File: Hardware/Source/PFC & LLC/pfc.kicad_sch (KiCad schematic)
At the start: 70 parts, among them J1 HB9500M-9.5-3P, K1 Relay 12VDC 10A, Q1 MMBT2222A, Q2 IPP60R125CP, Q3 MMBT2222A, U1 PC817X2NIPW, U2 OPAMP_OP07CSZ, U3 UCC28180D, U4 SN74LVC1G14DBVR

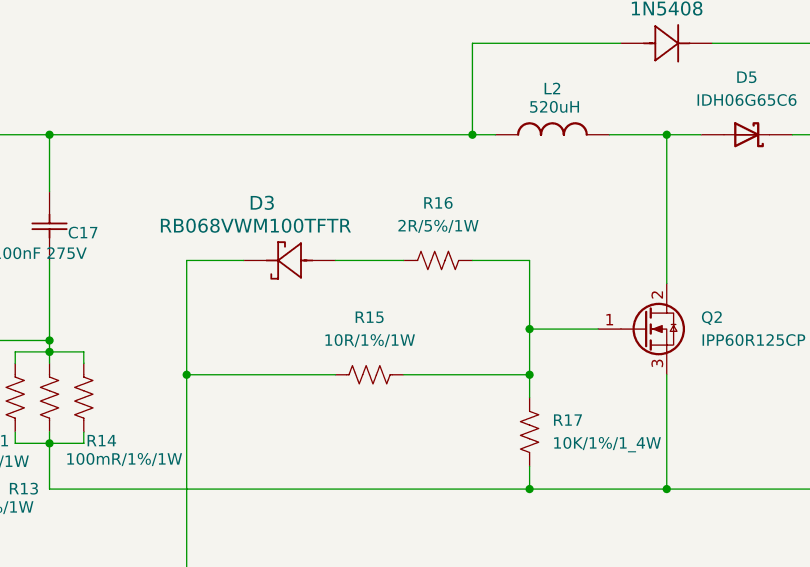
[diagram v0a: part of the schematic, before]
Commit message: Update PFC&LLC
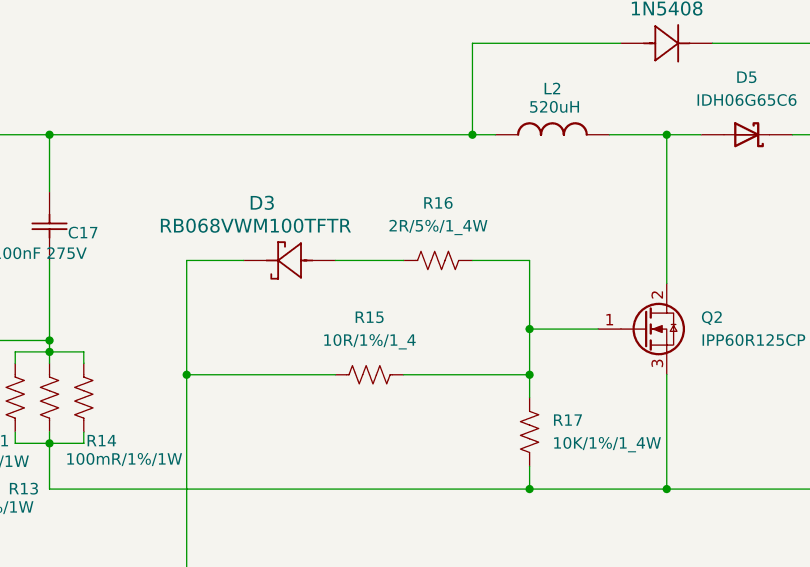
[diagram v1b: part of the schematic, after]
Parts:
- removed R15: 10R/1%/1W, charge_battery_footprint_lib:Res_2512, symbol charge_battery_sym_lib:Res_10R_2512_1%
- removed R16: 2R/5%/1W, charge_battery_footprint_lib:Res_2512, symbol charge_battery_sym_lib:Res_2R_2512_5%
- added R15: 10R/1%/1_4, charge_battery_footprint_lib:Res_1206, symbol charge_battery_sym_lib:Res_10R_1206_1%
- added R16: 2R/5%/1_4W, charge_battery_footprint_lib:Res_1206, symbol charge_battery_sym_lib:Res_2R_1206_1%
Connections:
- net at D3.1, U3.8 (GATE): now also R15.1
- net at D3.2: now also R16.1
- net at Q2.1 (G), R17.2: now also R15.2, R16.2
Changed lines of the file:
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@@
+	)
+	(symbol
+		(lib_id "charge_battery_sym_lib:Res_10R_1206_1%")
+		(at 313.69 105.41 0)
+		(unit 1)
+		(exclude_from_sim no)
+		(in_bom yes)
+		(on_board yes)
+		(dnp no)
+		(fields_autoplaced yes)
+		(property "Reference" "R15"
+			(at 317.5 99.06 0)
+			(effects
+				(font
+					(size 1.27 1.27)
+				)
+			)
+		)
+		(property "Value" "10R/1%/1_4"
+			(at 317.5 101.6 0)
+			(effects
+				(font
+					(size 1.27 1.27)
+				)
+			)
+		)
+		(property "Footprint" "charge_battery_footprint_lib:Res_1206"
+			(at 331.978 120.904 0)
+			(effects
+				(font
+					(size 1.27 1.27)
+				)
+				(hide yes)
+			)
+		)
+		(property "Datasheet" ""
+			(at 321.31 120.65 0)
+			(effects
+				(font
+					(size 1.27 1.27)
+				)
+				(hide yes)
+			)
+		)
+		(property "Description" "Res 10 Ohm 1206 1%"
+			(at 327.406 121.412 0)
+			(effects
+				(font
+					(size 1.27 1.27)
+				)
+				(hide yes)
+			)
+		)
+		(property "Supply name" "Thegioiic"
+			(at 332.994 121.158 0)
+			(effects
+				(font
+					(size 1.27 1.27)
+				)
+				(hide yes)
+			)
+		)
+		(property "Supply part number" "Điện Trở 10 Ohm 1206 1%"
+			(at 334.01 120.904 0)
+			(effects
+				(font
+					(size 1.27 1.27)
+				)
+				(hide yes)
+			)
+		)
+		(property "Supply URL" "https://www.thegioiic.com/dien-tro-10-ohm-1206-1-"
+			(at 341.122 122.174 0)
+			(effects
+				(font
+					(size 1.27 1.27)
+				)
+				(hide yes)
+			)
+		)
+		(pin "1"
+		)
+		(pin "2"
+		)
+		(instances
+			(project ""
+				(path "/97d1a1fe-d5a5-4da8-b78a-88a9132d14ad/bb0951d9-6e6a-40f4-8bc1-318f9d0bfafc"
+					(reference "R15")
+					(unit 1)
+				)
+			)
+		)
 	)
 	(symbol
@@
 	)
 	(symbol
+		(lib_id "charge_battery_sym_lib:Res_2R_1206_1%")
+		(at 325.12 88.9 0)
+		(unit 1)
+		(exclude_from_sim no)
+		(in_bom yes)
+		(on_board yes)
+		(dnp no)
+		(fields_autoplaced yes)
+		(property "Reference" "R16"
+			(at 325.12 86.36 0)
+			(effects
+				(font
+					(size 1.27 1.27)
+				)
+			)
+		)
+		(property "Value" "2R/5%/1_4W"
+			(at 325.12 88.9 0)
+			(effects
+				(font
+					(size 1.27 1.27)
+				)
+			)
+		)
+		(property "Footprint" "charge_battery_footprint_lib:Res_1206"
+			(at 325.12 88.9 0)
+			(effects
+				(font
+					(size 1.27 1.27)
+				)
+				(hide yes)
+			)
+		)
+		(property "Datasheet" ""
+			(at 325.12 88.9 0)
+			(effects
+				(font
+					(size 1.27 1.27)
+				)
+				(hide yes)
+			)
+		)
+		(property "Description" "Resistor 2 Ohm 1206 5%"
+			(at 325.12 88.9 0)
+			(effects
+				(font
+					(size 1.27 1.27)
+				)
+				(hide yes)
+			)
+		)
+		(property "Supply Name" "thegioiic"
+			(at 325.12 88.9 0)
+			(effects
+				(font
+					(size 1.27 1.27)
+				)
+				(hide yes)
+			)
+		)
+		(property "Supply Part Number" "Điện Trở 2 Ohm 1206 5%"
+			(at 325.12 88.9 0)
+			(effects
+				(font
+					(size 1.27 1.27)
+				)
+				(hide yes)
+			)
+		)
+		(property "Supply URL" "https://www.thegioiic.com/dien-tro-2-ohm-1206-5-"
+			(at 325.12 88.9 0)
+			(effects
+				(font
+					(size 1.27 1.27)
+				)
+				(hide yes)
+			)
+		)
+		(pin "1"
+		)
+		(pin "2"
+		)
+		(instances
+			(project ""
+				(path "/97d1a1fe-d5a5-4da8-b78a-88a9132d14ad/bb0951d9-6e6a-40f4-8bc1-318f9d0bfafc"
+					(reference "R16")
+					(unit 1)
+				)
+			)
+		)
+	)
+	(symbol
 		(lib_id "charge_battery_sym_lib:KBU1010 ")
 		(at 261.62 92.71 90)
@@
 				(path "/97d1a1fe-d5a5-4da8-b78a-88a9132d14ad/bb0951d9-6e6a-40f4-8bc1-318f9d0bfafc"
 					(reference "C1")
-					(unit 1)
-				)
-			)
-		)
-	)
-	(symbol
-		(lib_id "charge_battery_sym_lib:Res_2R_2512_5%")
-		(at 321.31 92.71 0)
-		(unit 1)
-		(exclude_from_sim no)
-		(in_bom yes)
-		(on_board yes)
-		(dnp no)
-		(fields_autoplaced yes)
-		(property "Reference" "R16"
-			(at 325.12 86.36 0)
-			(effects
-				(font
-					(size 1.27 1.27)
-				)
-			)
-		)
-		(property "Value" "2R/5%/1W"
-			(at 325.12 88.9 0)
-			(effects
-				(font
-					(size 1.27 1.27)
-				)
-			)
-		)
-		(property "Footprint" "charge_battery_footprint_lib:Res_2512"
-			(at 339.598 108.204 0)
-			(effects
-				(font
-					(size 1.27 1.27)
-				)
-				(hide yes)
-			)
-		)
-		(property "Datasheet" ""
-			(at 328.93 107.95 0)
-			(effects
-				(font
-					(size 1.27 1.27)
-				)
-				(hide yes)
-			)
-		)
-		(property "Description" "Res 2 Ohm 2512 1%"
-			(at 335.026 108.712 0)
-			(effects
-				(font
-					(size 1.27 1.27)
-				)
-				(hide yes)
-			)
-		)
-		(property "Supply name" "Thegioiic"
-			(at 340.614 108.458 0)
-			(effects
-				(font
-					(size 1.27 1.27)
-				)
-				(hide yes)
-			)
-		)
-		(property "Supply part number" "Điện Trở 2 Ohm 2512 1%"
-			(at 341.63 108.204 0)
-			(effects
-				(font
-					(size 1.27 1.27)
-				)
-				(hide yes)
-			)
-		)
-		(property "Supply URL" "https://www.thegioiic.com/dien-tro-2-ohm-2512-5-"
-			(at 348.742 109.474 0)
-			(effects
-				(font
-					(size 1.27 1.27)
-				)
-				(hide yes)
-			)
-		)
-		(pin "2"
-		)
-		(pin "1"
-		)
-		(instances
-			(project ""
-				(path "/97d1a1fe-d5a5-4da8-b78a-88a9132d14ad/bb0951d9-6e6a-40f4-8bc1-318f9d0bfafc"
-					(reference "R16")
 					(unit 1)
 				)
@@
 					(unit 1)
 				)
-			)
-		)
-	)
-	(symbol
-		(lib_id "charge_battery_sym_lib:Res_10R_2512_1%")
-		(at 313.69 105.41 0)
-		(unit 1)
-		(exclude_from_sim no)
-		(in_bom yes)
-		(on_board yes)
-		(dnp no)
-		(fields_autoplaced yes)
-		(property "Reference" "R15"
-			(at 317.5 99.06 0)
-			(effects
-				(font
-					(size 1.27 1.27)
-				)
-			)
-		)
-		(property "Value" "10R/1%/1W"
-			(at 317.5 101.6 0)
-			(effects
-				(font
-					(size 1.27 1.27)
-				)
-			)
-		)
-		(property "Footprint" "charge_battery_footprint_lib:Res_2512"
-			(at 331.978 120.904 0)
-			(effects
-				(font
-					(size 1.27 1.27)
-				)
-				(hide yes)
-			)
-		)
-		(property "Datasheet" ""
-			(at 321.31 120.65 0)
-			(effects
-				(font
-					(size 1.27 1.27)
-				)
-				(hide yes)
-			)
-		)
-		(property "Description" "Res 10 Ohm 2512 1%"
-			(at 327.406 121.412 0)
-			(effects
-				(font
-					(size 1.27 1.27)
-				)
-				(hide yes)
-			)
-		)
-		(property "Supply name" "Thegioiic"
-			(at 332.994 121.158 0)
-			(effects
-				(font
-					(size 1.27 1.27)
-				)
-				(hide yes)
-			)
-		)
-		(property "Supply part number" "Điện Trở 10 Ohm 2512 1%"
-			(at 334.01 120.904 0)
-			(effects
-				(font
-					(size 1.27 1.27)
-				)
-				(hide yes)
-			)
-		)
-		(property "Supply URL" "https://www.thegioiic.com/dien-tro-10-ohm-2512-1-"
-			(at 341.122 122.174 0)
-			(effects
-				(font
-					(size 1.27 1.27)
-				)
-				(hide yes)
-			)
-		)
-		(pin "2"
-		)
-		(pin "1"
-		)
-		(instances
-			(project ""
-				(path "/97d1a1fe-d5a5-4da8-b78a-88a9132d14ad/bb0951d9-6e6a-40f4-8bc1-318f9d0bfafc"
-					(reference "R15")
-					(unit 1)
-				)

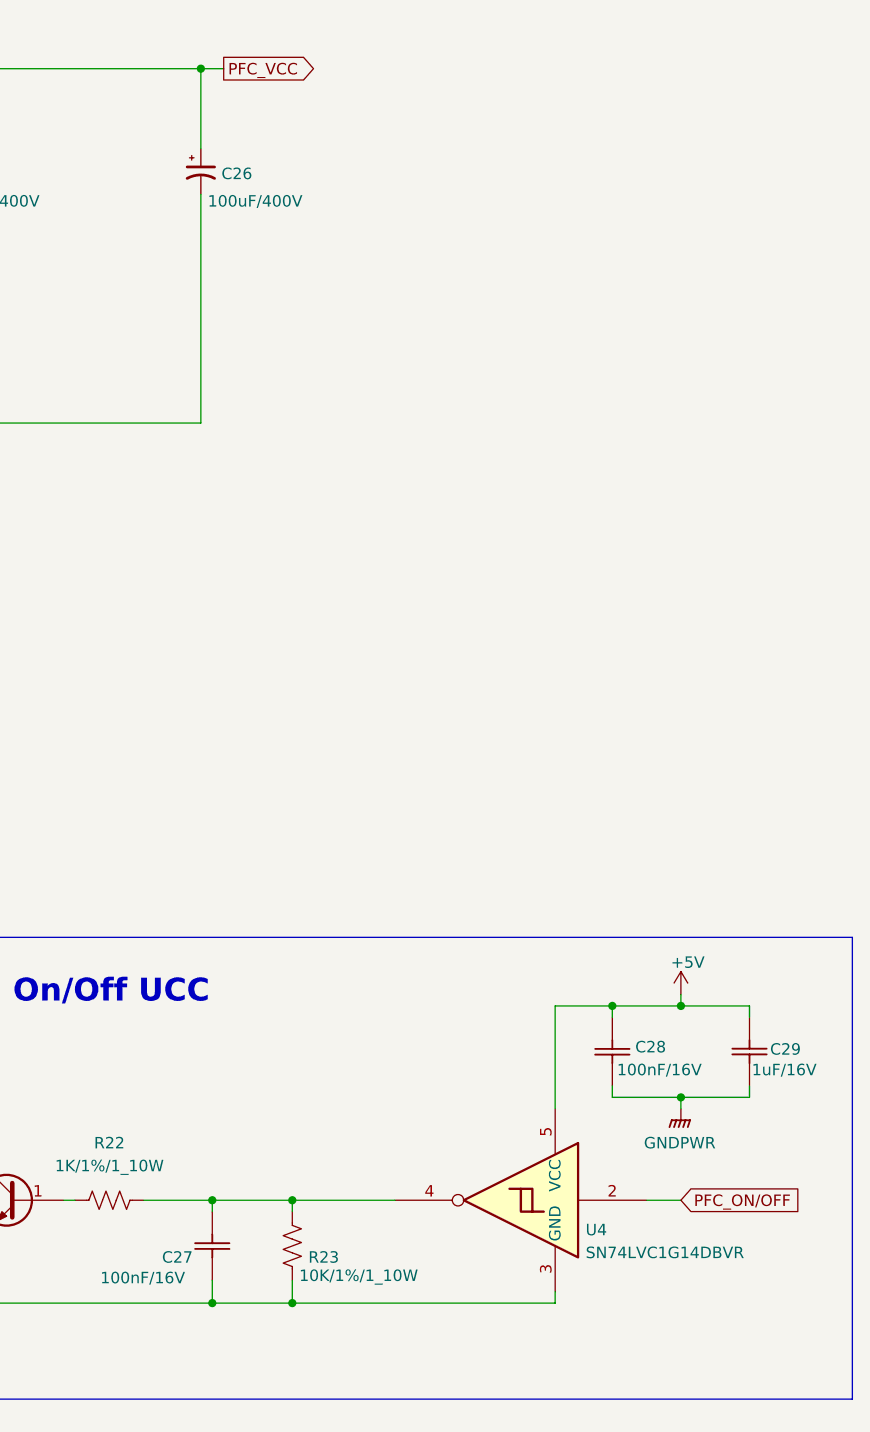
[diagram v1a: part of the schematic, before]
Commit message: Update PFC&LLC
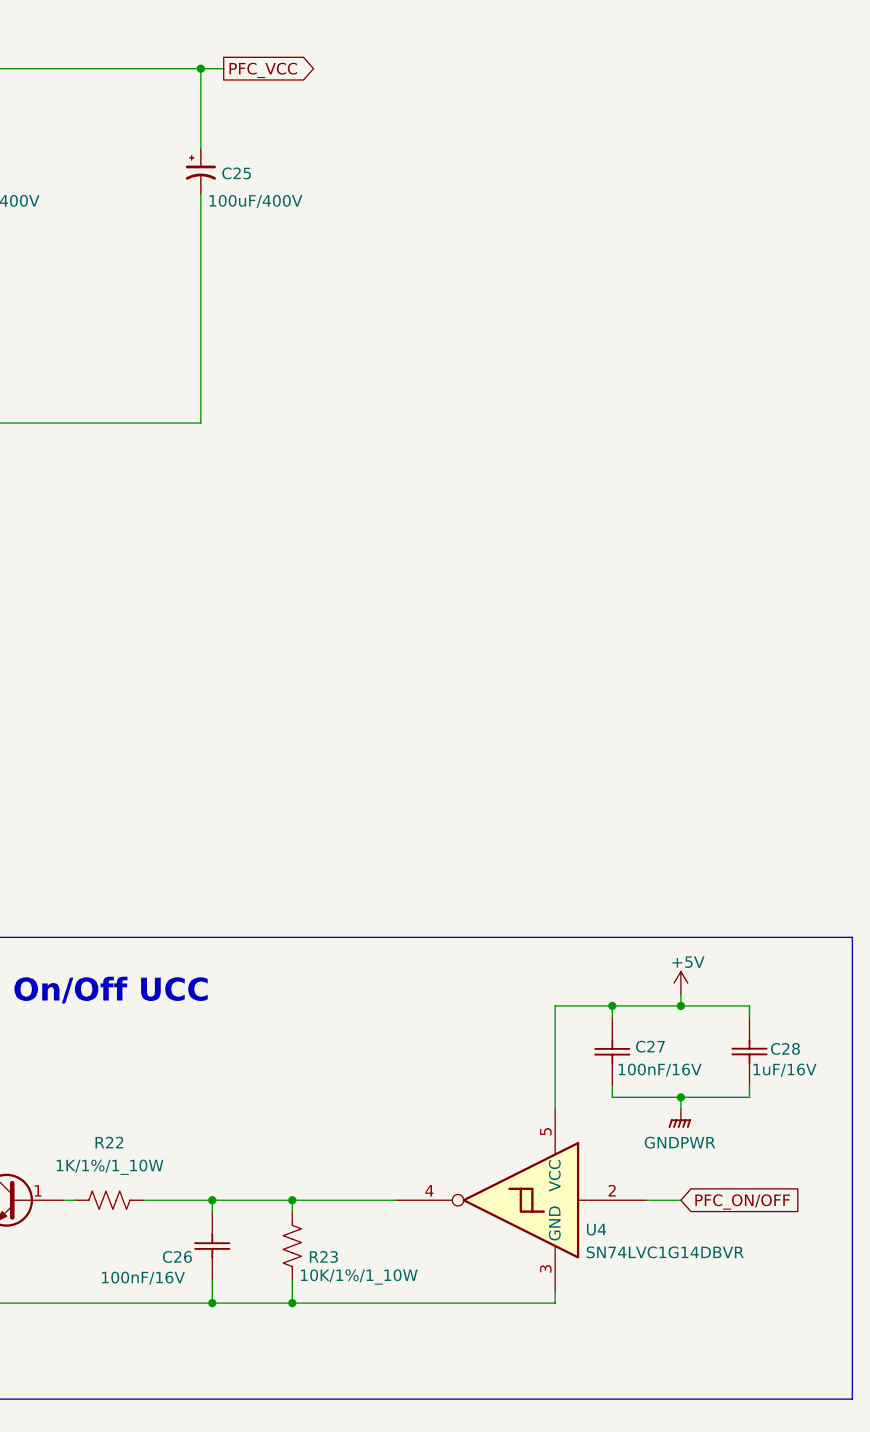
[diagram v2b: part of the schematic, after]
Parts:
- renumbered C26 to C25, C27 to C26, C28 to C27, C29 to C28
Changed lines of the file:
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@@
 		(on_board yes)
 		(dnp no)
-		(property "Reference" "C26"
+		(property "Reference" "C25"
 			(at 429.006 90.424 90)
 			(effects
@@
 			(project "PFC & LLC"
 				(path "/97d1a1fe-d5a5-4da8-b78a-88a9132d14ad/bb0951d9-6e6a-40f4-8bc1-318f9d0bfafc"
-					(reference "C26")
+					(reference "C25")
 					(unit 1)
 				)
@@
 		(on_board yes)
 		(dnp no)
-		(property "Reference" "C28"
+		(property "Reference" "C27"
 			(at 474.98 187.452 90)
 			(effects
@@
 			(project ""
 				(path "/97d1a1fe-d5a5-4da8-b78a-88a9132d14ad/bb0951d9-6e6a-40f4-8bc1-318f9d0bfafc"
-					(reference "C28")
+					(reference "C27")
 					(unit 1)
 				)
@@
 		(on_board yes)
 		(dnp no)
-		(property "Reference" "C29"
+		(property "Reference" "C28"
 			(at 489.966 187.706 90)
 			(effects
@@
 			(project ""
 				(path "/97d1a1fe-d5a5-4da8-b78a-88a9132d14ad/bb0951d9-6e6a-40f4-8bc1-318f9d0bfafc"
-					(reference "C29")
+					(reference "C28")
 					(unit 1)
 				)
@@
 		(on_board yes)
 		(dnp no)
-		(property "Reference" "C27"
+		(property "Reference" "C26"
 			(at 422.402 210.82 90)
 			(effects
@@
 			(project ""
 				(path "/97d1a1fe-d5a5-4da8-b78a-88a9132d14ad/bb0951d9-6e6a-40f4-8bc1-318f9d0bfafc"
-					(reference "C27")
+					(reference "C26")
 					(unit 1)
 				)

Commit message: Update lib: Choke in PFC Circuit
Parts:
- removed L1: SSRH24NH-45059, charge_battery_footprint_lib:SSRH24NH-45059, symbol charge_battery_sym_lib:SSRH24NH-45059
- added L1: SSRH24NH-45059, charge_battery_footprint_lib:TPCM-1.7-5, symbol charge_battery_sym_lib:TPCM-1.7-5
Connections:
- net AC2: now also L1.1
- net at C12.1, C5.2, D2.2: now also L1.4
- net at C12.2, C9.2, TH1.1: now also L1.3
- net at K1.3, R7.2: now also L1.2
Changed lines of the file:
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@@
 	)
 	(symbol
-		(lib_id "charge_battery_sym_lib:SSRH24NH-45059")
-		(at 199.39 110.49 90)
-		(unit 1)
-		(exclude_from_sim no)
-		(in_bom yes)
-		(on_board yes)
-		(dnp no)
-		(property "Reference" "L1"
-			(at 192.278 107.442 90)
-			(effects
-				(font
-					(size 1.524 1.524)
-				)
-				(justify right)
-			)
-		)
-		(property "Value" "SSRH24NH-45059"
-			(at 183.896 109.982 90)
-			(effects
-				(font
-					(size 1.524 1.524)
-				)
-				(justify right)
-			)
-		)
-		(property "Footprint" "charge_battery_footprint_lib:SSRH24NH-45059"
-			(at 219.456 111.252 0)
-			(effects
-				(font
-					(size 1.27 1.27)
-					(italic yes)
-				)
-				(hide yes)
-			)
-		)
-		(property "Datasheet" "https://www.mouser.vn/datasheet/2/447/KEM_LF0048_SSRH24NV_NH-3316880.pdf"
-			(at 219.202 105.918 0)
-			(effects
-				(font
-					(size 1.27 1.27)
-					(italic yes)
-				)
-				(hide yes)
-			)
-		)
-		(property "Description" "Common Mode Chokes / Filters 250VAC 5.9mH 4.5A 11.5mm DCR=48mOhms"
-			(at 219.456 108.712 0)
-			(effects
-				(font
-					(size 1.27 1.27)
-				)
-				(hide yes)
-			)
-		)
-		(property "Supply name" "Mouser"
-			(at 206.502 94.996 0)
-			(effects
-				(font
-					(size 1.27 1.27)
-				)
-				(hide yes)
-			)
-		)
-		(property "Supply part number" "80-SSRH24NH-45059"
-			(at 206.502 94.488 0)
-			(effects
-				(font
-					(size 1.27 1.27)
-				)
-				(hide yes)
-			)
-		)
-		(property "Supply URL" "https://www.mouser.vn/ProductDetail/KEMET/SSRH24NH-45059?qs=pfd5qewlna5bkXocAVZMGg%3D%3D"
-			(at 219.456 122.682 0)
-			(effects
-				(font
-					(size 1.27 1.27)
-				)
-				(hide yes)
-			)
-		)
-		(pin "2"
-		)
-		(pin "3"
-		)
-		(pin "4"
-		)
-		(pin "1"
-		)
-		(instances
-			(project ""
-				(path "/97d1a1fe-d5a5-4da8-b78a-88a9132d14ad/bb0951d9-6e6a-40f4-8bc1-318f9d0bfafc"
-					(reference "L1")
-					(unit 1)
-				)
-			)
-		)
-	)
-	(symbol
 		(lib_id "charge_battery_sym_lib:Ceramic_Cap_SMD_100nF_16V")
 		(at 207.01 260.35 90)
@@
 					(unit 1)
 				)
+			)
+		)
+	)
+	(symbol
+		(lib_id "charge_battery_sym_lib:TPCM-1.7-5")
+		(at 199.39 110.49 90)
+		(unit 1)
+		(exclude_from_sim no)
+		(in_bom no)
+		(on_board yes)
+		(dnp no)
+		(fields_autoplaced yes)
+		(property "Reference" "L1"
+			(at 203.2 93.9799 90)
+			(effects
+				(font
+					(size 1.524 1.524)
+				)
+				(justify right)
+			)
+		)
+		(property "Value" "SSRH24NH-45059"
+			(at 203.2 96.5199 90)
+			(effects
+				(font
+					(size 1.524 1.524)
+				)
+				(justify right)
+			)
+		)
+		(property "Footprint" "charge_battery_footprint_lib:TPCM-1.7-5"
+			(at 219.456 111.252 0)
+			(effects
+				(font
+					(size 1.27 1.27)
+					(italic yes)
+				)
+				(hide yes)
+			)
+		)
+		(property "Datasheet" "https://www.newark.com/pdfs/datasheets/Acme_Electric/TightPak.pdf"
+			(at 219.202 105.918 0)
+			(effects
+				(font
+					(size 1.27 1.27)
+					(italic yes)
+				)
+				(hide yes)
+			)
+		)
+		(property "Description" "Common Mode Chokes / Filters 250VAC 1.73mH 5A DCR=25mOhms"
+			(at 219.456 108.712 0)
+			(effects
+				(font
+					(size 1.27 1.27)
+				)
+				(hide yes)
+			)
+		)
+		(property "Supply name" "Mouser"
+			(at 206.502 94.996 0)
+			(effects
+				(font
+					(size 1.27 1.27)
+				)
+				(hide yes)
+			)
+		)
+		(property "Supply part number" ""
+			(at 206.502 94.488 0)
+			(effects
+				(font
+					(size 1.27 1.27)
+				)
+				(hide yes)
+			)
+		)
+		(property "Supply URL" "Thầy có"
+			(at 219.456 122.682 0)
+			(effects
+				(font
+					(size 1.27 1.27)
+				)
+				(hide yes)
+			)
+		)
+		(pin "1"
+		)
+		(pin "2"
+		)
+		(pin "4"
+		)
+		(pin "3"
+		)
+		(instances
+			(project ""
+				(path "/97d1a1fe-d5a5-4da8-b78a-88a9132d14ad/bb0951d9-6e6a-40f4-8bc1-318f9d0bfafc"
+					(reference "L1")
+					(unit 1)
+				)

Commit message: Exported BOM List 4 boards
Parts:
- C23, C24, C25, R16, R18, R19, R20: Supply name (none) -> Thegioiic
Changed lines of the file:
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@@
 			)
 		)
+		(property "Supply name" "Thegioiic"
+			(at 372.11 171.45 0)
+			(effects
+				(font
+					(size 1.27 1.27)
+				)
+				(hide yes)
+			)
+		)
 		(pin "2"
 		)
@@
 			)
 		)
+		(property "Supply name" "Thegioiic"
+			(at 383.54 87.63 0)
+			(effects
+				(font
+					(size 1.27 1.27)
+				)
+				(hide yes)
+			)
+		)
 		(pin "1"
 		)
@@
 			)
 		)
+		(property "Supply name" "Thegioiic"
+			(at 426.72 87.63 0)
+			(effects
+				(font
+					(size 1.27 1.27)
+				)
+				(hide yes)
+			)
+		)
 		(pin "1"
 		)
@@
 			)
 		)
+		(property "Supply name" "Thegioiic"
+			(at 372.11 156.21 0)
+			(effects
+				(font
+					(size 1.27 1.27)
+				)
+				(hide yes)
+			)
+		)
 		(pin "2"
 		)
@@
 			)
 		)
+		(property "Supply name" "Thegioiic"
+			(at 372.11 140.97 0)
+			(effects
+				(font
+					(size 1.27 1.27)
+				)
+				(hide yes)
+			)
+		)
 		(pin "2"
 		)
@@
 			)
 		)
+		(property "Supply name" "Thegioiic"
+			(at 325.12 88.9 0)
+			(effects
+				(font
+					(size 1.27 1.27)
+				)
+				(hide yes)
+			)
+		)
 		(pin "1"
 		)
@@
 			(effects
 				(font
+					(size 1.27 1.27)
+				)
+				(hide yes)
+			)
+		)
+		(property "Supply name" "Thegioiic"
+			(at 397.51 87.63 0)
+			(effects
+				(font
